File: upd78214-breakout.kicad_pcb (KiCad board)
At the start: 2 copper layers, 1 part, among them U1 upd78214-64p-qfp

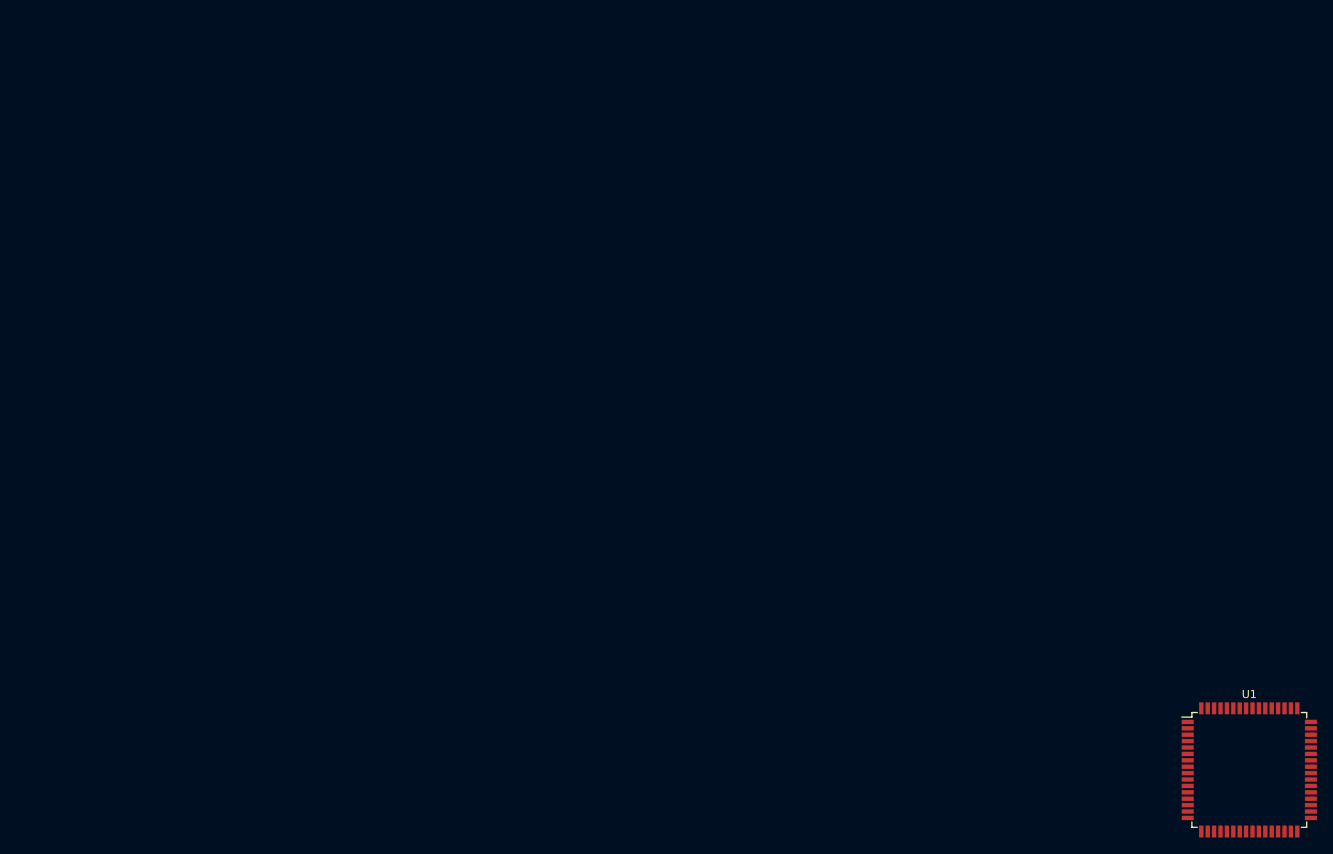
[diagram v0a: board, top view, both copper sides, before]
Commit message: NEC footprint, Toshiba symbol
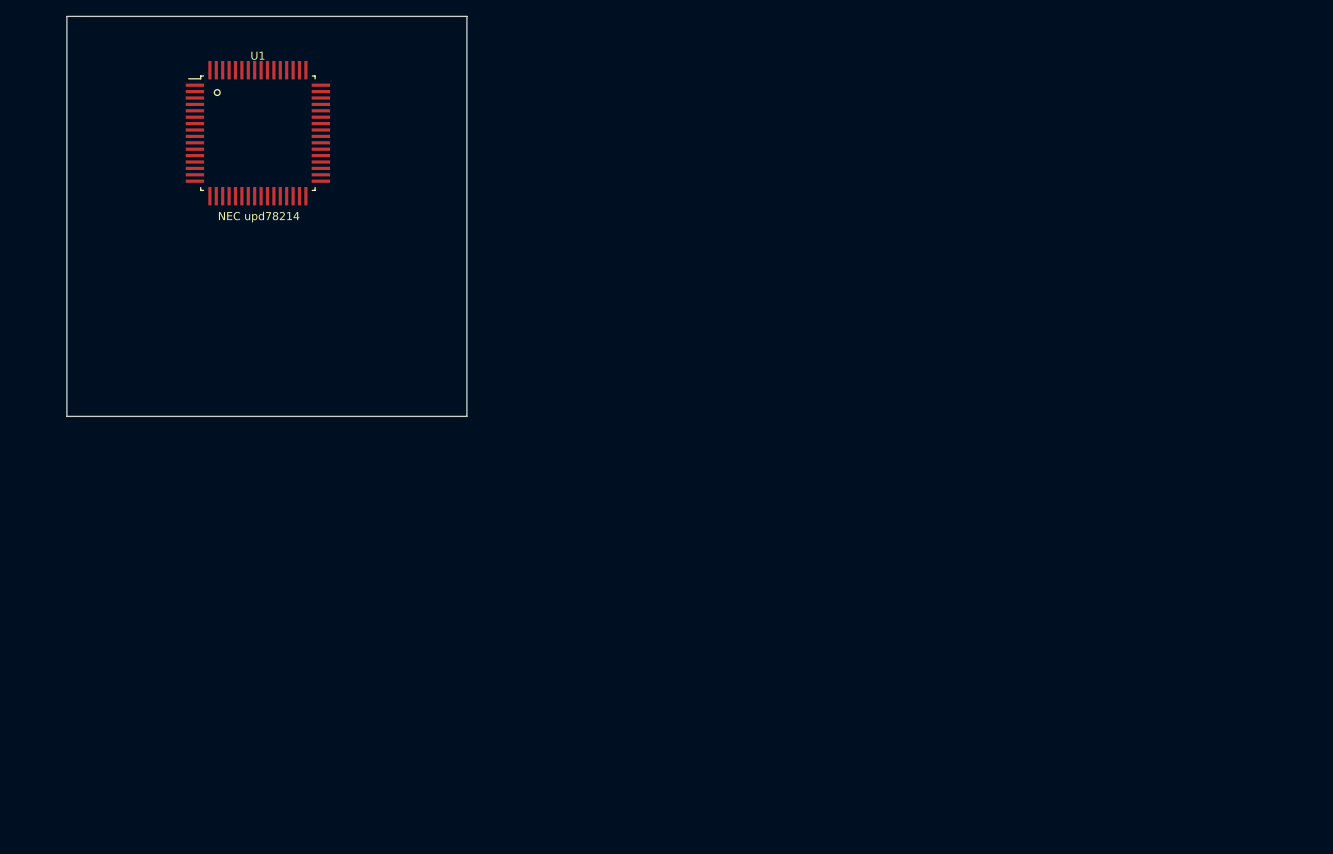
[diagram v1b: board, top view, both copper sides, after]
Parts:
- U1: footprint Package_QFP:TQFP-64_14x14mm_P0.8mm -> NEC:QFP-64_14x14_Pitch0.8mm
- moved U1 147.3 mm to (103.9, 93.6)
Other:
- board outline added: 50 x 50 mm
- board text added: "NEC upd78214"

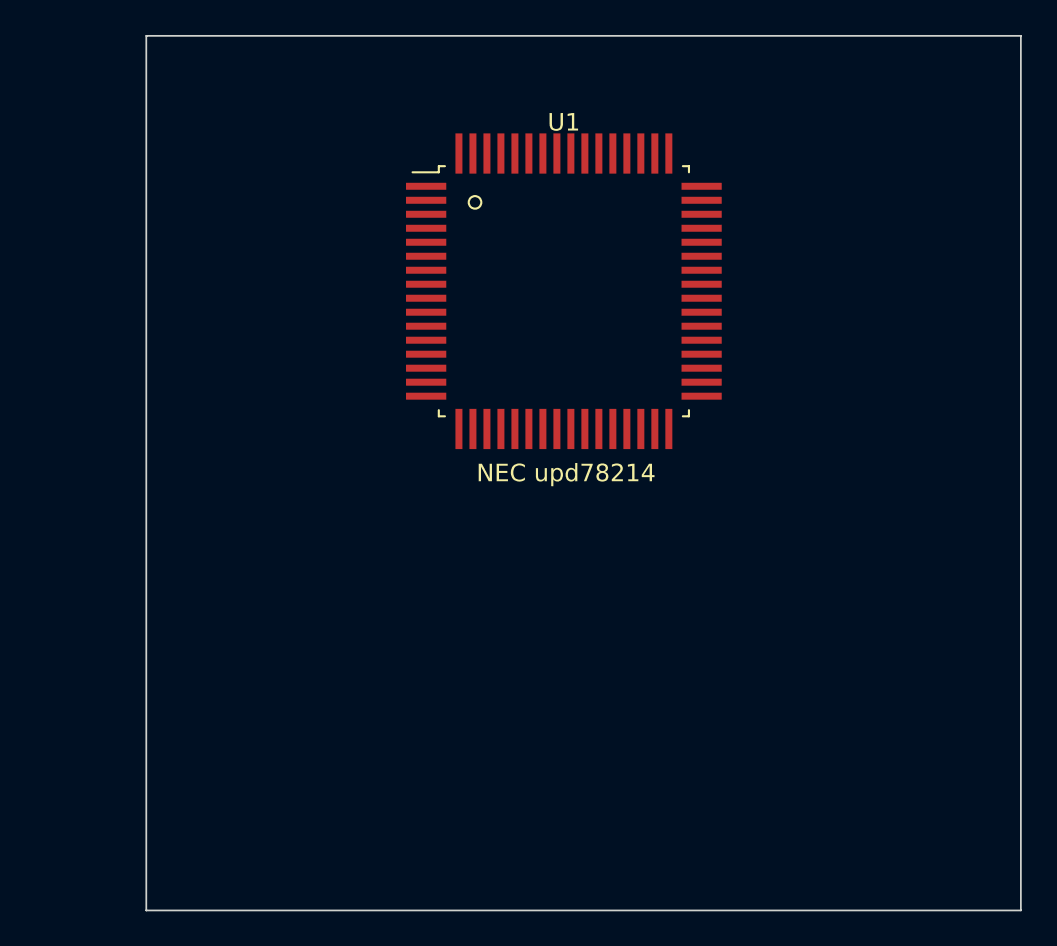
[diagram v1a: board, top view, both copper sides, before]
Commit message: USB power for test board
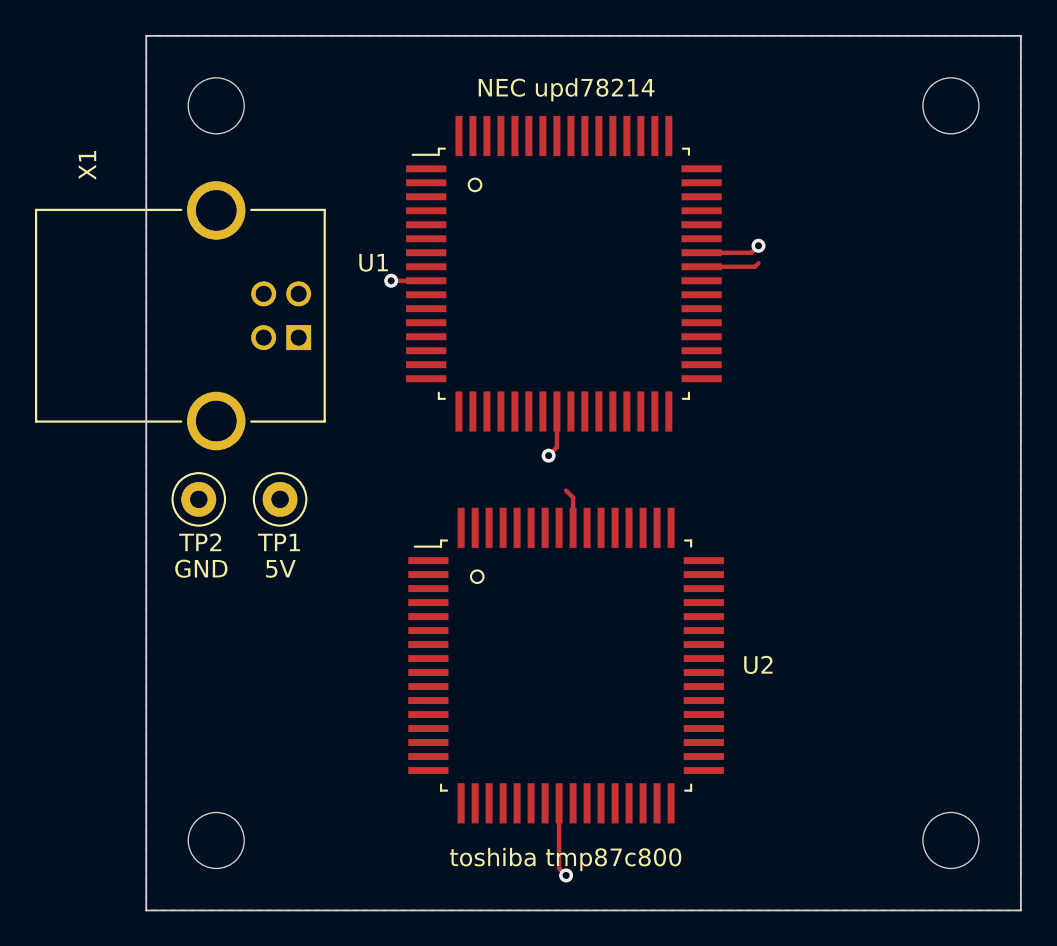
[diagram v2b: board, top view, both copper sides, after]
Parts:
- added REF**: MountingHole_3.2mm_M3, MountingHole:MountingHole_3.2mm_M3, F.Cu at (84.0, 125.0)
- added REF**: MountingHole_3.2mm_M3, MountingHole:MountingHole_3.2mm_M3, F.Cu at (84.0, 83.0)
- added REF**: MountingHole_3.2mm_M3, MountingHole:MountingHole_3.2mm_M3, F.Cu at (126.0, 125.0)
- added REF**: MountingHole_3.2mm_M3, MountingHole:MountingHole_3.2mm_M3, F.Cu at (126.0, 83.0)
- added TP1: 5V, TestPoint:TestPoint_Loop_D2.50mm_Drill1.0mm, F.Cu at (87.7, 105.5)
- added TP2: GND, TestPoint:TestPoint_Loop_D2.50mm_Drill1.0mm, F.Cu at (83.0, 105.5)
- added U2: tmp87c800df, NEC:QFP-64_14x14_Pitch0.8mm, F.Cu at (104.0, 115.0)
- added X1: USB-B1HSB6, USB-B1HSB6:OST_USB-B1HSB6, F.Cu at (84.0, 95.0)
- moved U1 1.00 mm to (103.9, 92.6)
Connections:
- U1 pad 24: unconnected-(U1-Pad24) -> GND
- U1 pad 41: unconnected-(U1-Pad41) -> +5V
- U1 pad 42: unconnected-(U1-Pad42) -> GND
- U1 pad 9: unconnected-(U1-Pad9) -> GND
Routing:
- net GND: track 0.00 -> 12.4 mm, vias 0 -> 4
- net +5V: track 0.00 -> 5.63 mm
- added copper zone on F.Cu, net +5V
- added copper zone on B.Cu, net GND
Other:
- board text added: "2022 leadedsolder.com"
- board text added: "playdia project breakout board v0.1"
- board text added: "toshiba tmp87c800"
